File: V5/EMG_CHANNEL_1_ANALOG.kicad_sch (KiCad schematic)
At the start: 34 parts, among them J301 AudioJack3 TRS, U301 INA333xxDGK, U302 MCP6004

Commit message: fix channel 1 analog polarity and block rectifier placeholder
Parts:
- removed D301, D302: BAS70/BAT54, symbol Device:D_Schottky
- removed R333: 10k matched, symbol Device:R
- R332: value 10k matched -> 1M R_RECT_PLACEHOLDER
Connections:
- net EMG1_ENV_DRV: now also U302.13 (-); no longer U302.12 (+)
- net EMG1_IN_N_PROT: now also U301.2 (-); no longer U301.3 (+)
- net EMG1_IN_P: now also J301.T; no longer J301.S
- net EMG1_IN_P_PROT: now also U301.3 (+); no longer U301.2 (-)
- net EMG1_RECT_DRV: now also R332.2; no longer U302.7
- net EMG1_REF_ELECTRODE: now also J301.S; no longer J301.T
- net ENV_LPF_NODE: now also U302.12 (+); no longer U302.13 (-)
- net RAW_GAIN_FB: now also U302.2 (-); no longer U302.3 (+)
- net RAW_HPF_NODE: now also U302.3 (+); no longer U302.2 (-)
- net U302C_RESERVED: now also U302.9 (-); no longer U302.10 (+)
- net analog VREF: now also R332.1, U302.10 (+), U302.5 (+); no longer U302.9 (-)
- net RECT_ABS_IN renamed U302B_RESERVED
- net U302B_RESERVED: now also U302.7; no longer R332.1
- removed net RECT_FB: R332.2, U302.5 (+)
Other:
- note added: "4) RECT BLOCKED PLACEHOLDER"
- note added: "ENV placeholder follows EMG1_RECT_DRV; ENV is not functional until RECT is implemented."
- note added: "Not a functional rectifier. Do not duplicate to Channel 2 or PCB until topology is selected."
- note added: "RECT topology blocked: EMG1_RECT_DRV temporarily biased to analog VREF via R332 (1M)."
- note removed: "4) RECT CANDIDATE"
- note removed: "EMG1_RECT candidate = analog VREF + abs(EMG1_RAW - analog VREF)."
- note removed: "Envelope LPF candidate: R341 = 33k, C341 = 1uF to analog VREF."
- note removed: "Topology candidate; bench validation required."

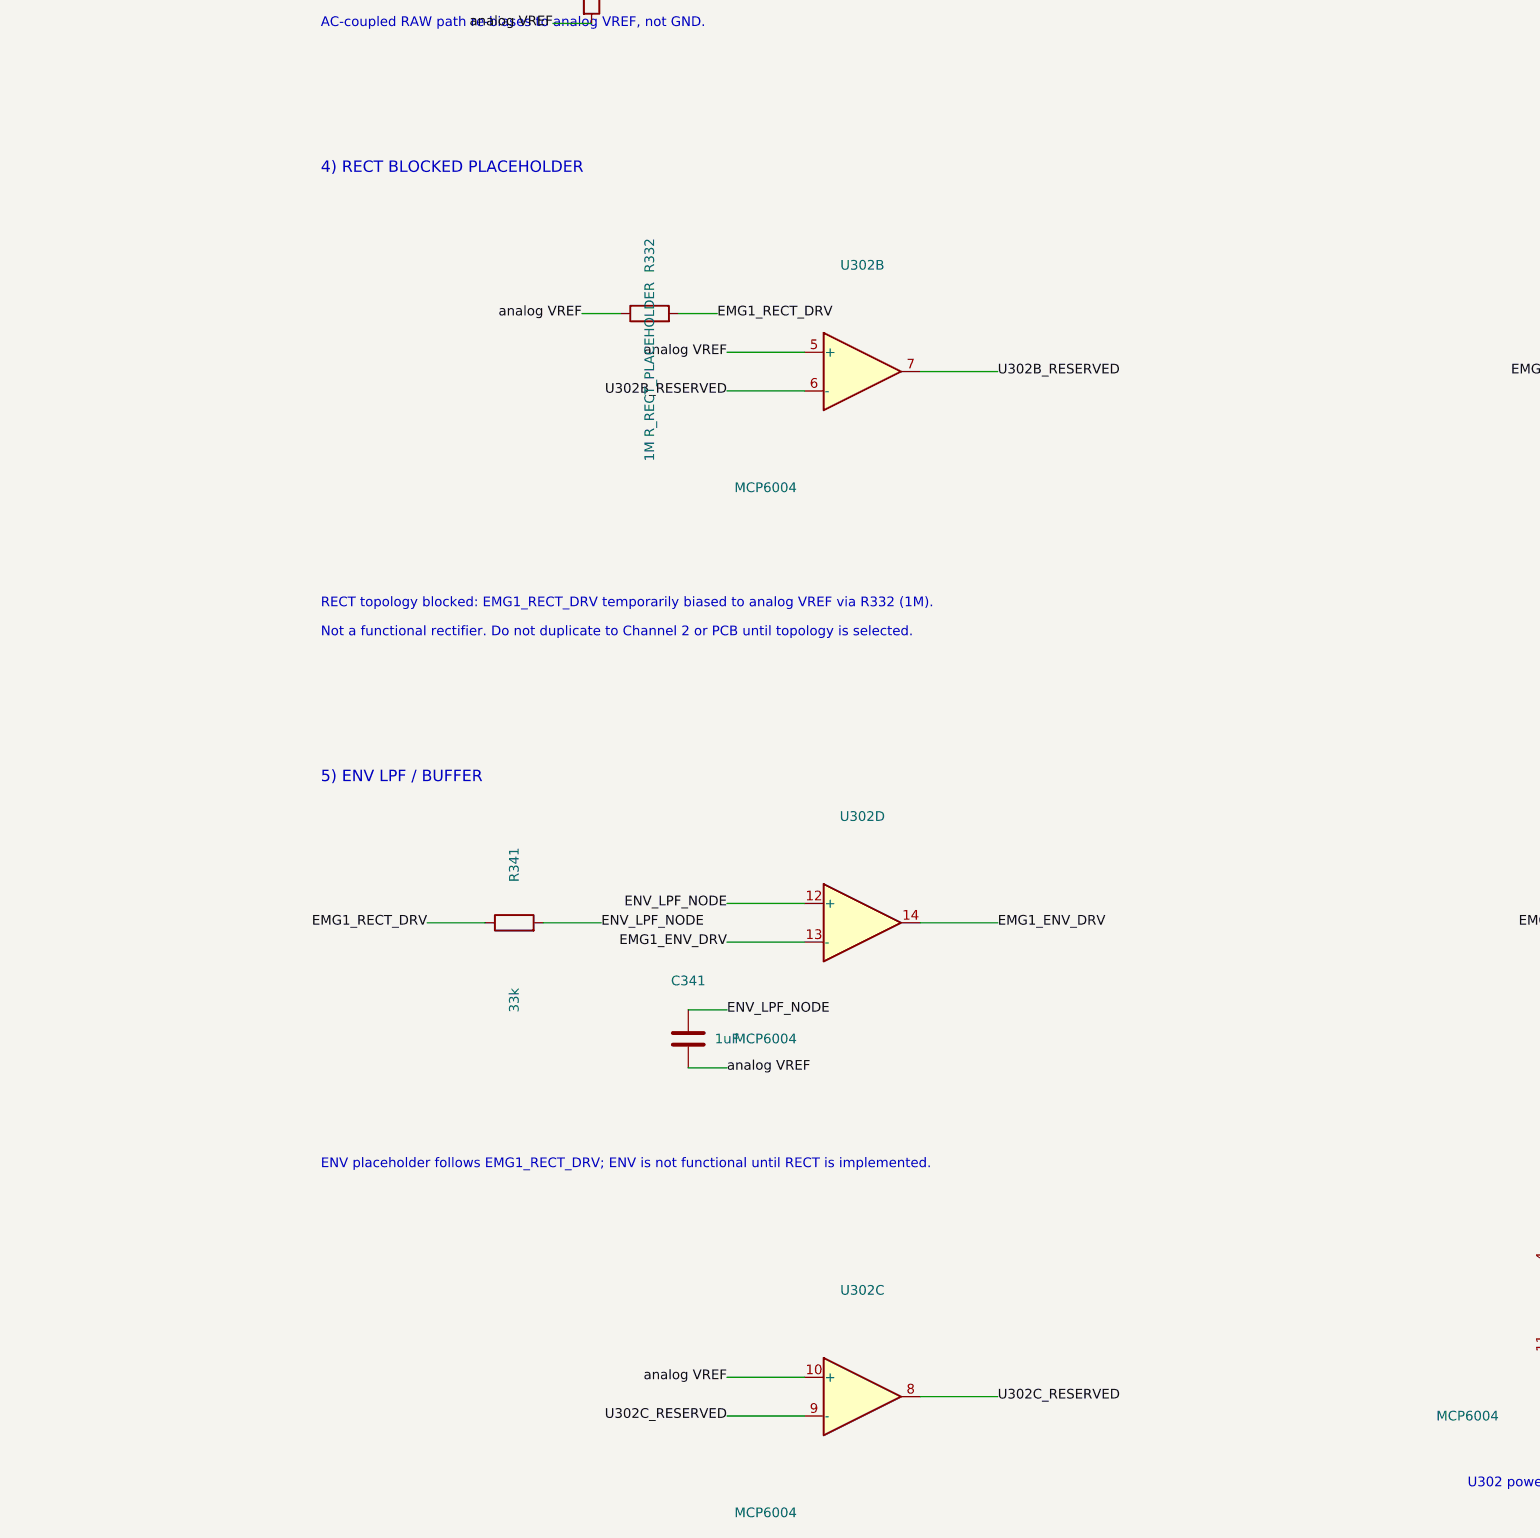
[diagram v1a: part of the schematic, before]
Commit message: implement channel 1 rectifier candidate
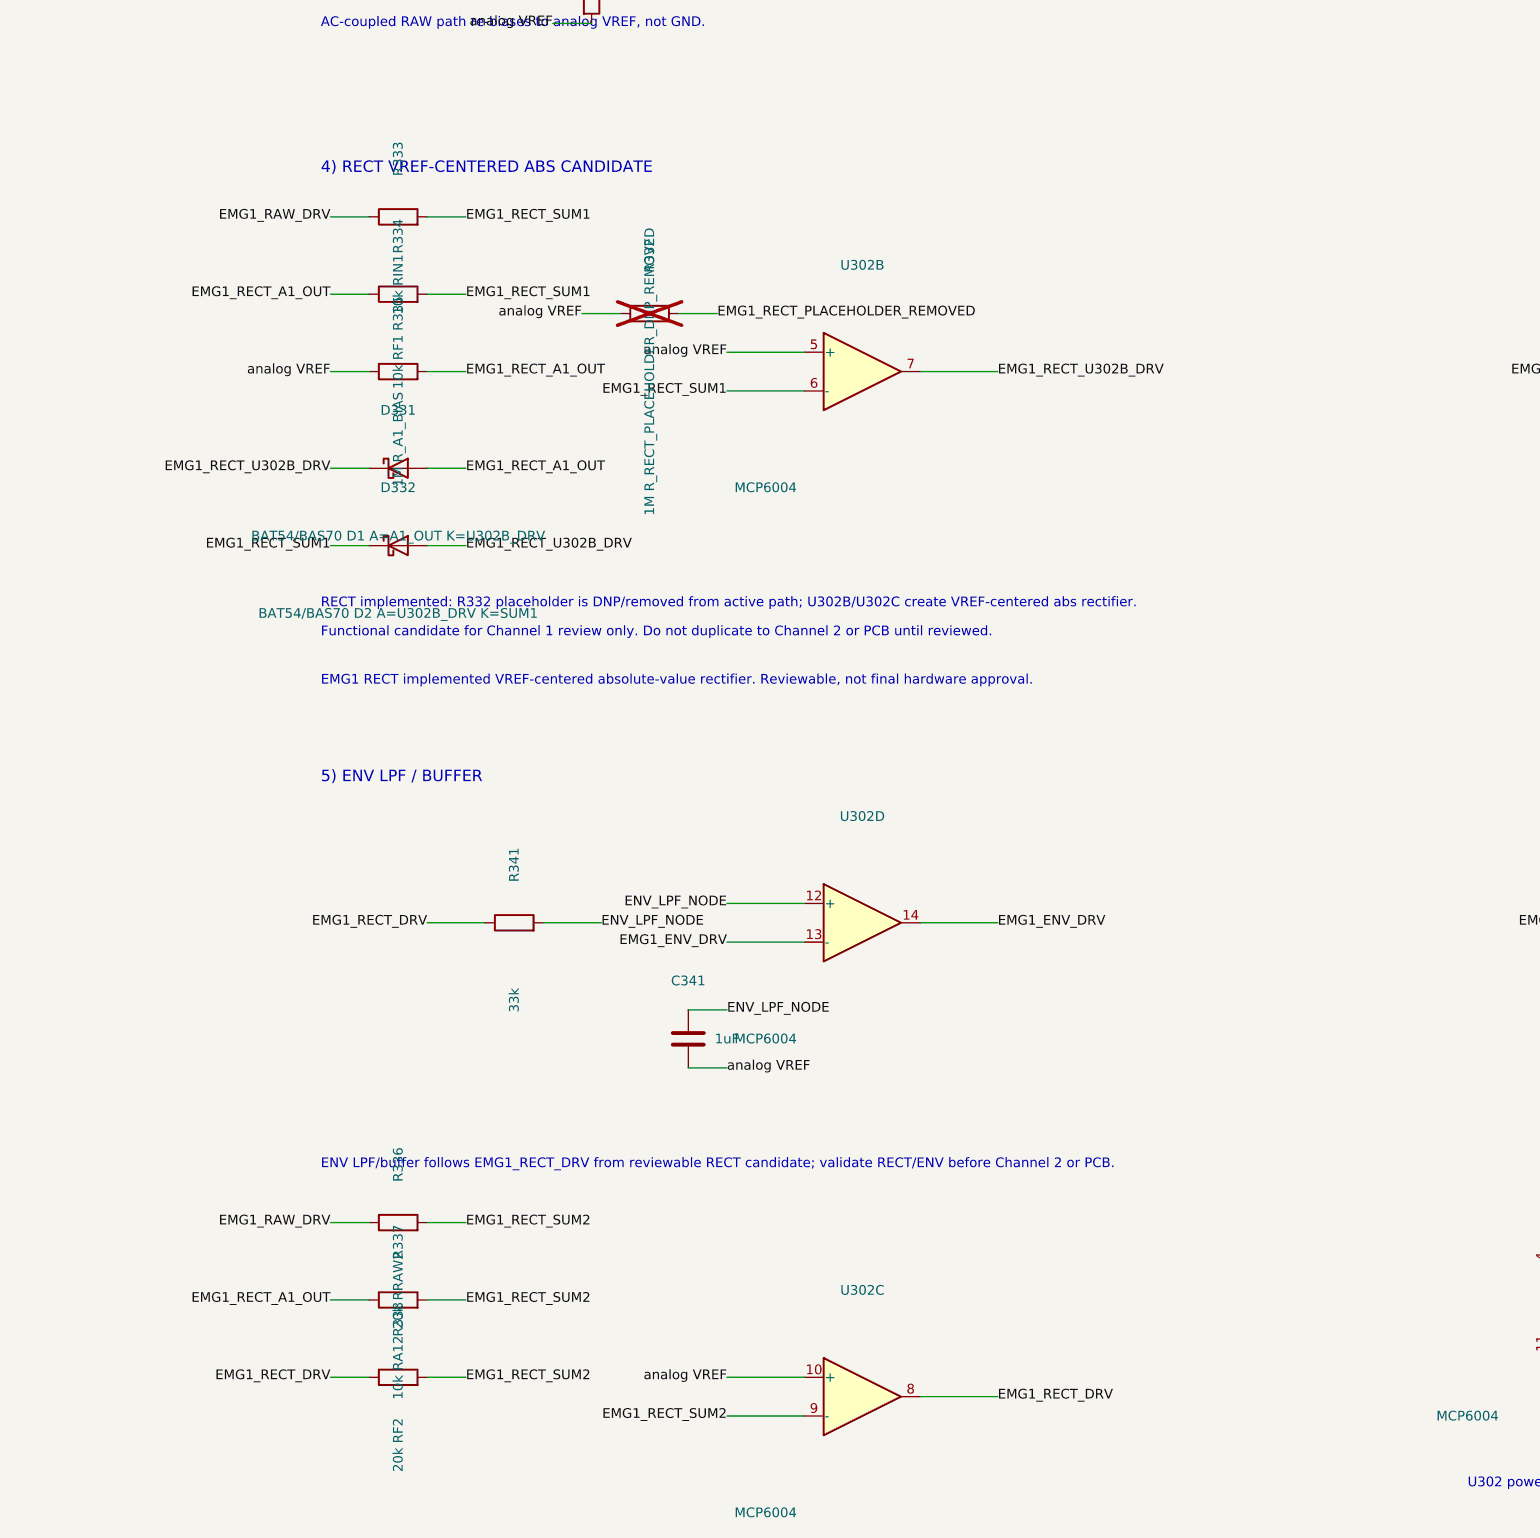
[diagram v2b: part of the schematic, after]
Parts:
- added D331: BAT54/BAS70 D1 A=A1_OUT K=U302B_DRV, symbol Device:D_Schottky
- added D332: BAT54/BAS70 D2 A=U302B_DRV K=SUM1, symbol Device:D_Schottky
- added R333: 10k RIN1, symbol Device:R
- added R334: 10k RF1, symbol Device:R
- added R335: 1M R_A1_BIAS, symbol Device:R
- added R336: 20k RRAW2, symbol Device:R
- added R337: 10k RA12, symbol Device:R
- added R338: 20k RF2, symbol Device:R
- R332: value 1M R_RECT_PLACEHOLDER -> 1M R_RECT_PLACEHOLDER_DNP_REMOVED; now not fitted; now left out of the parts list
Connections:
- net EMG1_RAW_DRV: now also R333.1, R336.1
- net EMG1_RECT_DRV: now also U302.8, R338.1; no longer R332.2
- net analog VREF: now also R335.1
- net U302B_RESERVED renamed EMG1_RECT_SUM1
- net EMG1_RECT_SUM1: now also D332.1 (K), R333.2, R334.2; no longer U302.7
- net U302C_RESERVED renamed EMG1_RECT_SUM2
- net EMG1_RECT_SUM2: now also R336.2, R337.2, R338.2; no longer U302.8
- new net EMG1_RECT_A1_OUT: D331.2 (A), R334.1, R335.2, R337.1
- new net EMG1_RECT_PLACEHOLDER_REMOVED: R332.2
- new net EMG1_RECT_U302B_DRV: D331.1 (K), D332.2 (A), U302.7
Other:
- note added: "4) RECT VREF-CENTERED ABS CANDIDATE"
- note added: "EMG1 RECT implemented VREF-centered absolute-value rectifier. Reviewable, not final hardware approval."
- note added: "ENV LPF/buffer follows EMG1_RECT_DRV from reviewable RECT candidate; validate RECT/ENV before Channel 2 or PCB."
- note added: "Functional candidate for Channel 1 review only. Do not duplicate to Channel 2 or PCB until reviewed."
- note added: "RECT implemented: R332 placeholder is DNP/removed from active path; U302B/U302C create VREF-centered abs rectifier."
- note removed: "4) RECT BLOCKED PLACEHOLDER"
- note removed: "ENV placeholder follows EMG1_RECT_DRV; ENV is not functional until RECT is implemented."
- note removed: "Not a functional rectifier. Do not duplicate to Channel 2 or PCB until topology is selected."
- note removed: "RECT topology blocked: EMG1_RECT_DRV temporarily biased to analog VREF via R332 (1M)."

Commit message: cleanup channel 1 rectifier schematic readability
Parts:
- removed R332: 1M R_RECT_PLACEHOLDER_DNP_REMOVED, symbol Device:R
- D331: value BAT54/BAS70 D1 A=A1_OUT K=U302B_DRV -> BAT54/BAS70
- D332: value BAT54/BAS70 D2 A=U302B_DRV K=SUM1 -> BAT54/BAS70
- R333: value 10k RIN1 -> 10k
- R334: value 10k RF1 -> 10k
- R335: value 1M R_A1_BIAS -> 1M
- R336: value 20k RRAW2 -> 20k
- R337: value 10k RA12 -> 10k
- R338: value 20k RF2 -> 20k
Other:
- note added: "ADC/output caps: C321/C331 = 1nF to GND; C351 = 4.7nF to GND."
- note added: "D331/D332 orientation notes: D331 A=A1_OUT K=U302B_DRV; D332 A=U302B_DRV K=SUM1."
- note added: "ENV LPF storage: C341 = 1uF from ENV_LPF_NODE to analog VREF."
- note added: "RECT implemented: U302B/U302C create reviewable VREF-centered abs rectifier."
- note added: "RECT resistor roles: R333/R334/R337 = 10k; R336/R338 = 20k; R335 = 1M bias."
- note removed: "470R series per output. RAW/RECT caps = 1nF to GND. ENV cap = 4.7nF to GND."
- note removed: "ENV LPF/buffer follows EMG1_RECT_DRV from reviewable RECT candidate; validate RECT/ENV before Channel 2 or PCB."
- note removed: "RECT implemented: R332 placeholder is DNP/removed from active path; U302B/U302C create VREF-centered abs rectifier."
- moved on the sheet: C301, C302, C303, C304, C310, C311, C314, C321, C331, C341, C351, C360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

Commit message: assign channel 1 rectifier footprints
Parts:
- C321, C331, C341, C351, C360: footprint (none) -> Capacitor_SMD:C_0805_2012Metric
- D331, D332: footprint (none) -> Diode_SMD:D_SOD-123
- R333, R334, R335, R336, R337, R338: footprint (none) -> Resistor_SMD:R_0805_2012Metric
- U302: footprint (none) -> Package_DIP:DIP-14_W7.62mm
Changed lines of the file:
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@@
 			)
 		)
-		(property "Footprint" ""
+		(property "Footprint" "Resistor_SMD:R_0805_2012Metric"
 			(at 276.86 269.24 0)
 			(hide yes)
@@
 			)
 		)
-		(property "Footprint" ""
+		(property "Footprint" "Diode_SMD:D_SOD-123"
 			(at 276.86 180.34 0)
 			(hide yes)
@@
 			)
 		)
-		(property "Footprint" ""
+		(property "Footprint" "Resistor_SMD:R_0805_2012Metric"
 			(at 276.86 147.32 0)
 			(hide yes)
@@
 			)
 		)
-		(property "Footprint" ""
+		(property "Footprint" "Resistor_SMD:R_0805_2012Metric"
 			(at 276.86 157.48 0)
 			(hide yes)
@@
 			)
 		)
-		(property "Footprint" ""
+		(property "Footprint" "Resistor_SMD:R_0805_2012Metric"
 			(at 276.86 289.56 0)
 			(hide yes)
@@
 			)
 		)
-		(property "Footprint" ""
+		(property "Footprint" "Resistor_SMD:R_0805_2012Metric"
 			(at 276.86 279.4 0)
 			(hide yes)
@@
 			)
 		)
-		(property "Footprint" ""
+		(property "Footprint" "Diode_SMD:D_SOD-123"
 			(at 276.86 170.18 0)
 			(hide yes)
@@
 			)
 		)
-		(property "Footprint" ""
+		(property "Footprint" "Package_DIP:DIP-14_W7.62mm"
 			(at 322.58 73.66 0)
 			(hide yes)
@@
 			)
 		)
-		(property "Footprint" ""
+		(property "Footprint" "Package_DIP:DIP-14_W7.62mm"
 			(at 337.82 157.48 0)
 			(hide yes)
@@
 			)
 		)
-		(property "Footprint" ""
+		(property "Footprint" "Capacitor_SMD:C_0805_2012Metric"
 			(at 256.54 251.46 0)
 			(hide yes)
@@
 			)
 		)
-		(property "Footprint" ""
+		(property "Footprint" "Package_DIP:DIP-14_W7.62mm"
 			(at 337.82 229.87 0)
 			(hide yes)
@@
 			)
 		)
-		(property "Footprint" ""
+		(property "Footprint" "Package_DIP:DIP-14_W7.62mm"
 			(at 278.13 306.07 0)
 			(hide yes)
@@
 			)
 		)
-		(property "Footprint" ""
+		(property "Footprint" "Package_DIP:DIP-14_W7.62mm"
 			(at 420.37 165.1 0)
 			(hide yes)
@@
 			)
 		)
-		(property "Footprint" ""
+		(property "Footprint" "Capacitor_SMD:C_0805_2012Metric"
 			(at 457.2 165.1 0)
 			(hide yes)
@@
 			)
 		)
-		(property "Footprint" ""
+		(property "Footprint" "Capacitor_SMD:C_0805_2012Metric"
 			(at 434.34 67.31 0)
 			(hide yes)
@@
 			)
 		)
-		(property "Footprint" ""
+		(property "Footprint" "Capacitor_SMD:C_0805_2012Metric"
 			(at 467.36 107.95 0)
 			(hide yes)
@@
 			)
 		)
-		(property "Footprint" ""
+		(property "Footprint" "Capacitor_SMD:C_0805_2012Metric"
 			(at 464.82 133.35 0)
 			(hide yes)
@@
 			)
 		)
-		(property "Footprint" ""
+		(property "Footprint" "Resistor_SMD:R_0805_2012Metric"
 			(at 276.86 137.16 0)
 			(hide yes)

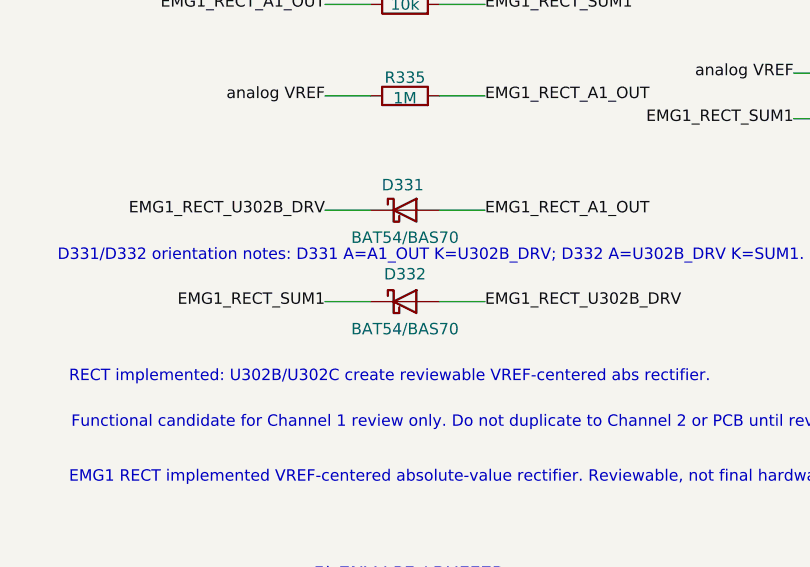
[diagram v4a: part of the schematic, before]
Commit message: clarify channel 1 rectifier diode values
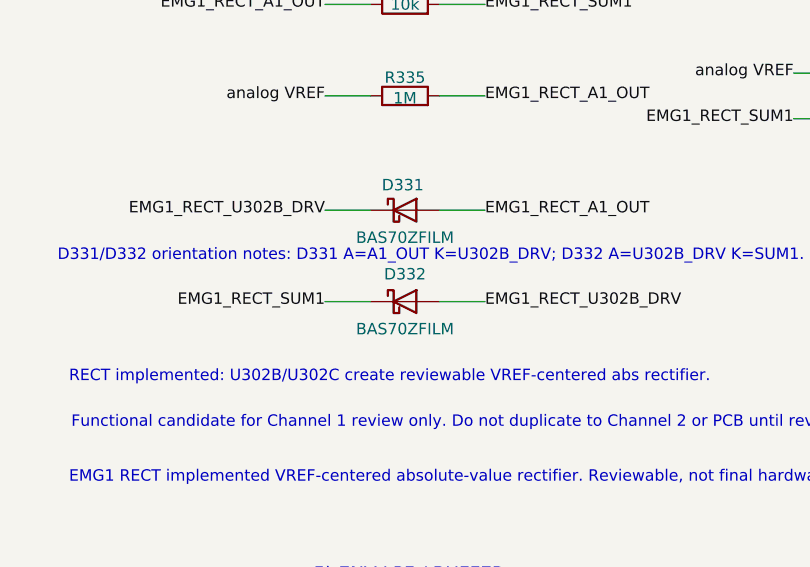
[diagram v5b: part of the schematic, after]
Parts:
- D331, D332: value BAT54/BAS70 -> BAS70ZFILM
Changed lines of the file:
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@@
 			)
 		)
-		(property "Value" "BAT54/BAS70"
+		(property "Value" "BAS70ZFILM"
 			(at 276.86 183.388 0)
 			(show_name no)
@@
 			)
 		)
-		(property "Value" "BAT54/BAS70"
+		(property "Value" "BAS70ZFILM"
 			(at 276.86 173.228 0)
 			(show_name no)

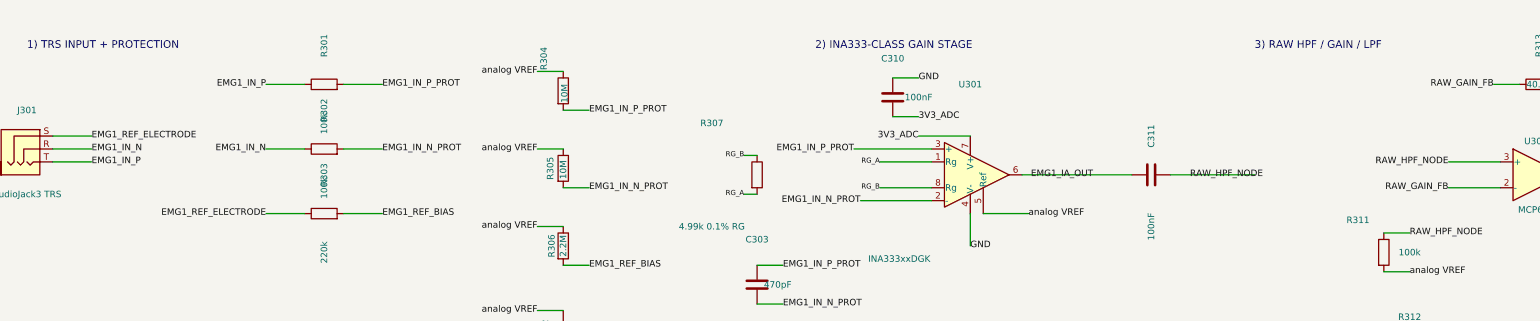
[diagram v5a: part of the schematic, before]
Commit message: fix channel trs mapping and raw gain input polarity
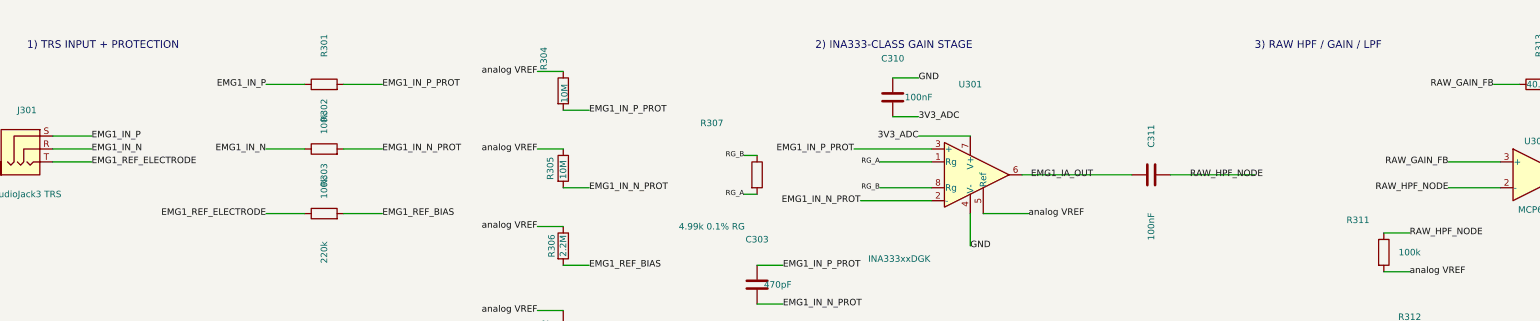
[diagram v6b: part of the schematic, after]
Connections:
- net EMG1_IN_P: now also J301.S; no longer J301.T
- net EMG1_REF_ELECTRODE: now also J301.T; no longer J301.S
- net RAW_GAIN_FB: now also U302.3 (+); no longer U302.2 (-)
- net RAW_HPF_NODE: now also U302.2 (-); no longer U302.3 (+)
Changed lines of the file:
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@@
 		)
 	)
-	(label "EMG1_REF_ELECTRODE"
+	(label "EMG1_IN_P"
 		(at 38.1 66.04 0)
 		(effects
@@
 		)
 	)
-	(label "EMG1_IN_P"
+	(label "EMG1_REF_ELECTRODE"
 		(at 38.1 71.12 0)
 		(effects
@@
 		)
 	)
+	(label "RAW_HPF_NODE"
+		(at 304.8 76.2 180)
+		(effects
+			(font
+				(size 1.27 1.27)
+			)
+			(justify right)
+		)
+	)
 	(label "RAW_GAIN_FB"
-		(at 304.8 76.2 180)
-		(effects
-			(font
-				(size 1.27 1.27)
-			)
-			(justify right)
-		)
-	)
-	(label "RAW_HPF_NODE"
 		(at 304.8 71.12 180)
 		(effects
